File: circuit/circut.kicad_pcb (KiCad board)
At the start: 2 copper layers, 124 x 159 mm, 12 parts, among them J1 ESP321, J3 Conn_02x04_Top_Bottom

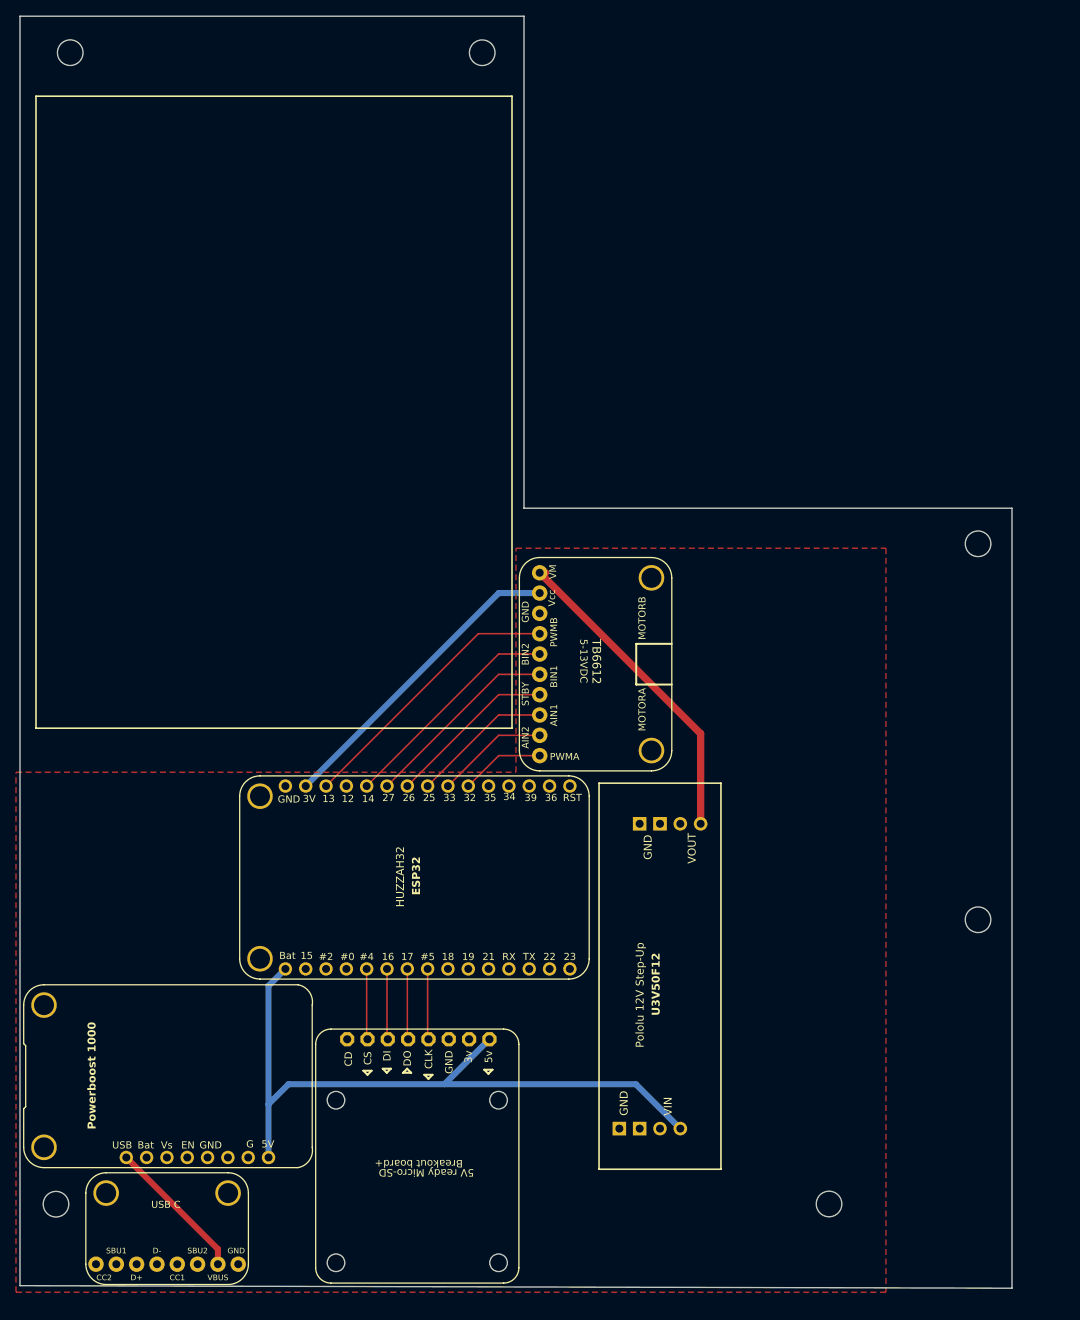
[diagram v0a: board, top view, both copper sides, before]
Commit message: updating carrier board design
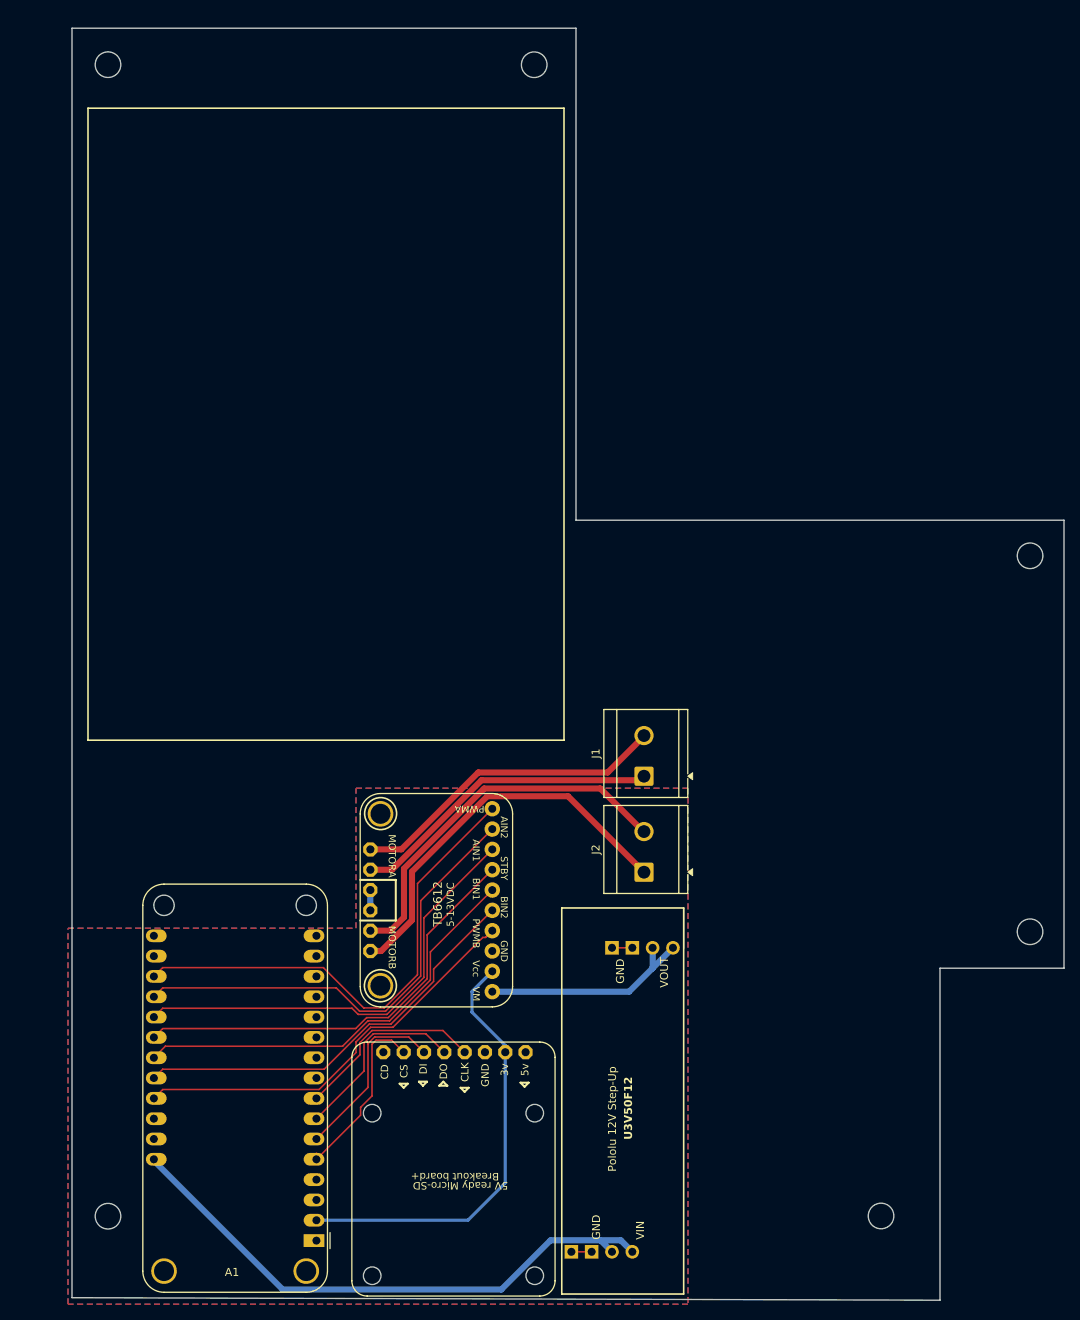
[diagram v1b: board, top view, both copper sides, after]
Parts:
- removed Motor-In1: Conn_01x10, Library:Adafruit TB6612
- removed Powerboost1: Conn_01x08, Library:Adafruit Powerboost 1000
- removed USBC1: Conn_01x08, Library:Adafruit USB-C Breakout
- added A1: Adafruit_Feather_HUZZAH32_ESP32, Module:Adafruit_Feather_WithMountingHoles, F.Cu at (66.1, 178.1)
- added J2: Screw_Terminal_01x02, TerminalBlock_CUI:TerminalBlock_CUI_TB007-508-02_1x02_P5.08mm_Horizontal, F.Cu at (107.0, 132.0)
- added U1: TB6612FNG, Library:Adafruit TB6612, F.Cu at (73.5, 135.7)
- J1: value ESP321 -> Screw_Terminal_01x02; footprint Library:Adafruit_Huzzah32_breakout -> TerminalBlock_CUI:TerminalBlock_CUI_TB007-508-02_1x02_P5.08mm_Horizontal
- moved J1 44.9 mm to (107.0, 120.0), turned to 90 degrees
- moved J3 15.9 mm to (110.6, 141.4)
- moved REF** 6.67 mm to (136.6, 175.0)
- moved REF** 6.67 mm to (93.3, 31.1)
- moved REF** 6.67 mm to (155.3, 92.4)
- moved REF** 6.67 mm to (155.3, 139.4)
- moved REF** 6.67 mm to (40.0, 175.0)
- moved REF** 4.95 mm to (40.0, 31.1)
- moved SD1 4.80 mm to (92.2, 154.5)
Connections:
- J1 pad 1: /Battery -> Net-(J1-Pin_1)
- J1 pad 2: unconnected-(J1-Pin_2-Pad2) -> Net-(J1-Pin_2)
- J3 pad 1: unconnected-(J3-Pin_1-Pad1) -> GND
- J3 pad 3: unconnected-(J3-Pin_3-Pad3) -> /Battery
- J3 pad 5: unconnected-(J3-Pin_5-Pad5) -> GND
- J3 pad 7: unconnected-(J3-Pin_7-Pad7) -> /12v
- SD1 pad 1: /Battery -> unconnected-(SD1-Pin_1-Pad1)
- SD1 pad 2: unconnected-(SD1-Pin_2-Pad2) -> /3v
- SD1 pad 4: /CLK -> Net-(A1-I39/A3)
- SD1 pad 5: /DO -> Net-(A1-I34/A2)
- SD1 pad 6: /DI -> Net-(A1-DAC1/A1)
- SD1 pad 7: /CS -> Net-(A1-DAC2/A0)
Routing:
- net /PWMB: track 0.00 -> 51.8 mm
- net /PWMA: track 10.5 -> 61.8 mm
- net Net-(J2-Pin_1): track 0.00 -> 49.7 mm
- net Net-(J2-Pin_2): track 0.00 -> 47.4 mm
- net /AIN2: track 14.1 -> 58.9 mm
- net Net-(J1-Pin_2): track 0.00 -> 40.1 mm
- net Net-(J1-Pin_1): track 0.00 -> 39.0 mm
- net /AIN1: track 17.7 -> 56.0 mm
- net /GPIO13: track 34.6 -> 0.00 mm
- net /STBY: track 21.3 -> 54.2 mm
- net /BIN1: track 24.9 -> 53.0 mm
- net Net-(A1-I39/A3): track 0.00 -> 24.1 mm
- net /BIN2: track 28.5 -> 51.9 mm
- net Net-(A1-I34/A2): track 0.00 -> 23.4 mm
- net Net-(A1-DAC2/A0): track 0.00 -> 22.8 mm
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- added copper zone on B.Cu, net GND
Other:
- outline, holes or cut-outs redrawn
